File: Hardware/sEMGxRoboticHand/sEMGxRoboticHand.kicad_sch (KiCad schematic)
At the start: 49 parts, among them U1 ADS1298xPAG, U2 ESP32-S3, U3 ADS1298xPAG

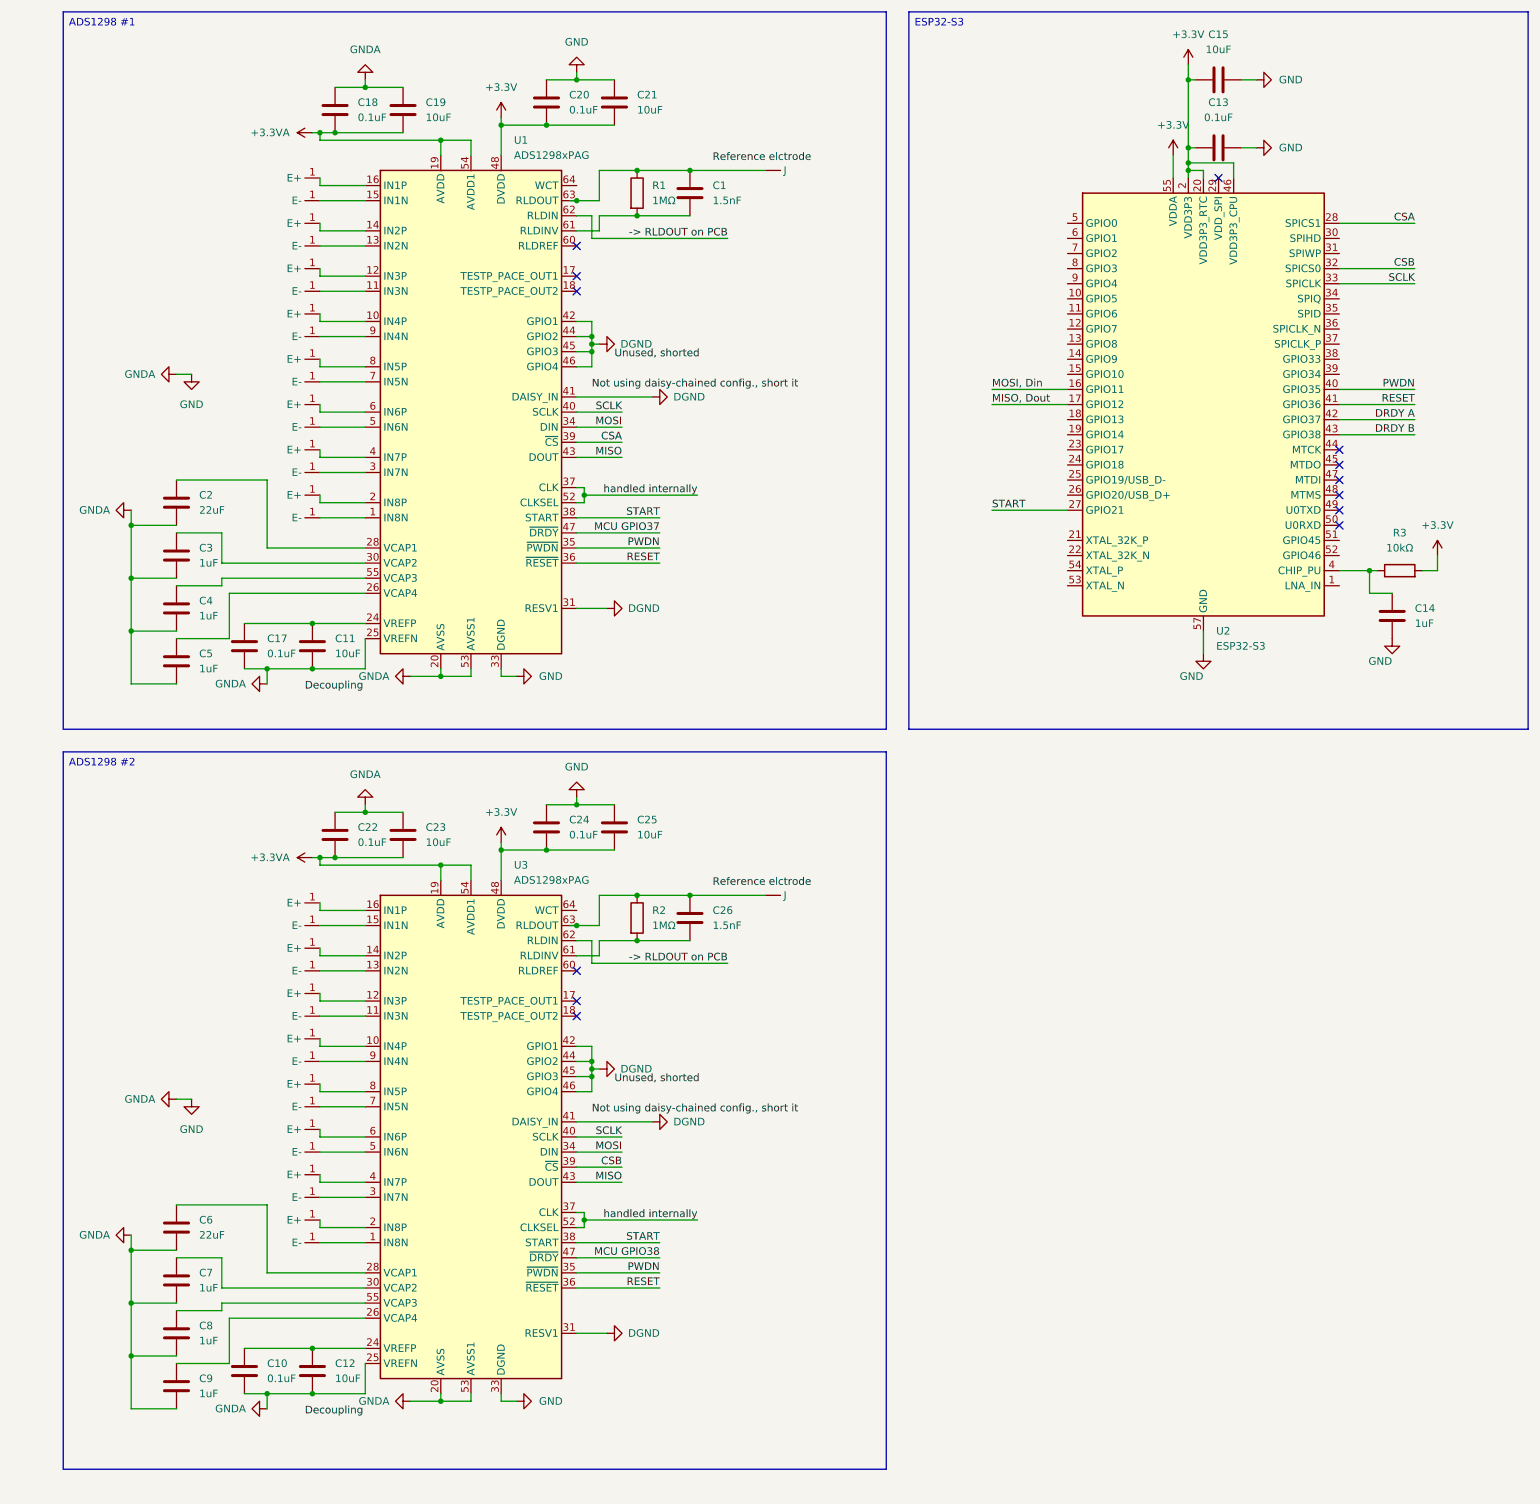
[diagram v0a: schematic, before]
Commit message: [style] Update Design
- Update labelling of "GNDA" to "AGND"
- Update arrow pointing directions of GNDs and Voltage supplies following convention
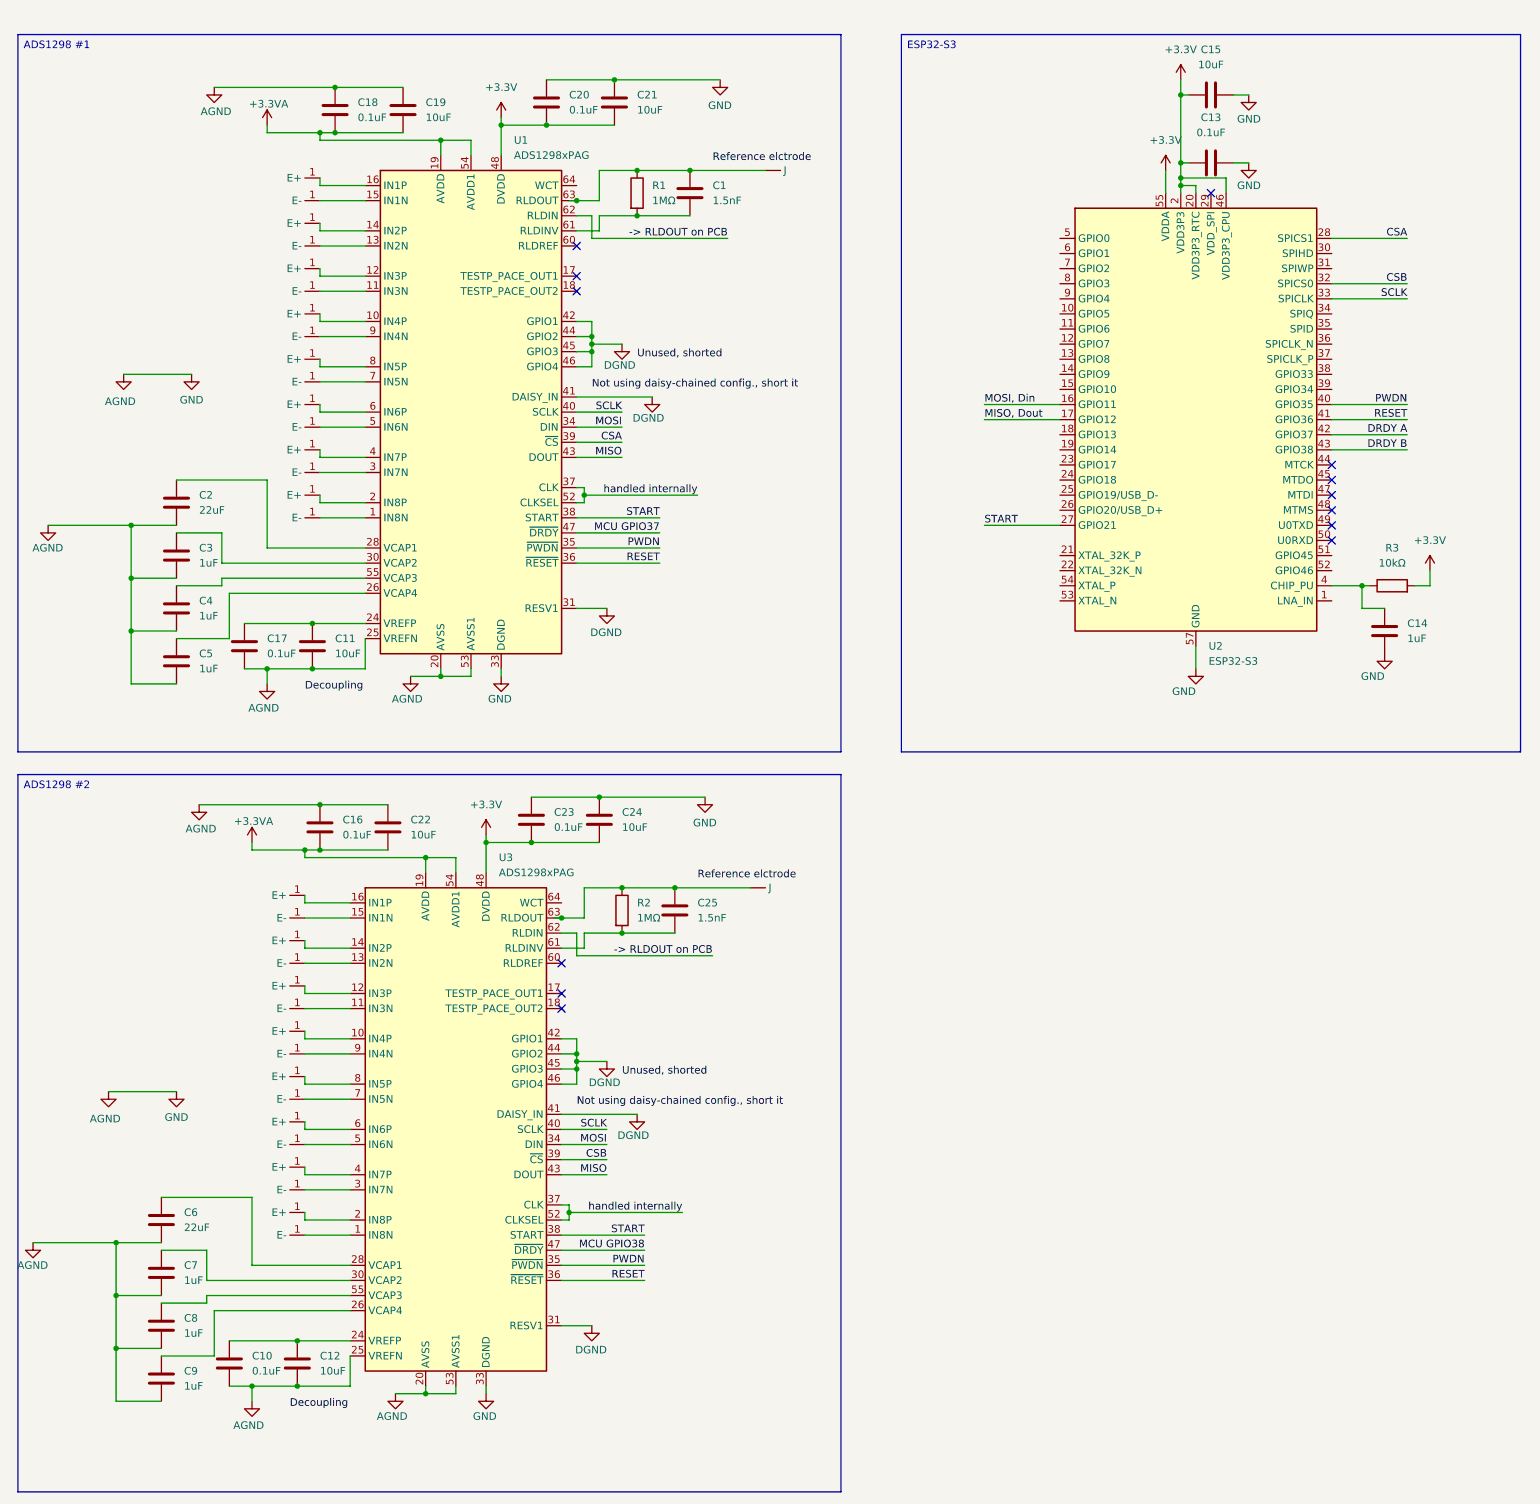
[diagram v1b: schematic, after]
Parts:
- removed C26: 1.5nF, symbol Device:C
- added C16: 0.1uF, symbol Device:C
- C22, C24: value 0.1uF -> 10uF
- C23: value 10uF -> 0.1uF
- C25: value 10uF -> 1.5nF
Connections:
- net +3.3V: now also C23.2; no longer C25.2
- net +3.3VA: now also C16.2; no longer C23.2
- net at R2.1, U3.63 (RLDOUT), U5. (J): now also C25.1
- net at R2.2, U3.61 (RLDINV): now also C25.2
- net GND renamed AGND
- net AGND: now also C16.1; no longer C25.1
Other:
- moved on the sheet: C13, C14, C15, R3, U2

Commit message: [style] Update labels & ports & texts
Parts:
- removed E1: ~, symbol dry_electrode:differential_electrode
- added C26: C, symbol Device:C
- added R4: R, symbol Device:R
- added U6: ESP32-S3-WROOM-1, RF_Module:ESP32-S3-WROOM-1, symbol RF_Module:ESP32-S3-WROOM-1
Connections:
- net MCU GPIO37 is gone; now on net DRDY A: U1.47 (~{DRDY})
- net MCU GPIO38 is gone; now on net DRDY B: U3.47 (~{DRDY})
- net MISO, Dout is gone; now on net MISO: U2.17 (GPIO12)
- net MOSI, Din is gone; now on net MOSI: U2.16 (GPIO11)
- net at U1.15 (IN1N): now also C26.2
- net at U1.16 (IN1P): now also C26.1, R4.2
- net -> RLDOUT on PCB: no longer names the net of U3.62 (RLDIN)
- net -> RLDOUT on PCB: no longer U1.62 (RLDIN)
- net handled internally: no longer names the net of U3.37 (CLK), U3.52 (CLKSEL)
- net handled internally: no longer U1.37 (CLK), U1.52 (CLKSEL)
- new net: U6.1 (GND), U6.40 (GND), U6.41 (GND)
- new net: U1.37 (CLK), U1.52 (CLKSEL)
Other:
- note added: "Not using daisy-chained config., short it"
- note added: "RLDIN -> RLDOUT on PCB"
- note added: "Reference elctrode"
- note added: "Unused, shorted"
- note added: "handled internally"
- moved on the sheet: C1, C11, C13, C14, C15, C17, C18, C19, C2, C20, C21, C3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

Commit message: [style] Replace electrodes to components
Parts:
- removed E2, E3, E4, E5, E6, E7, E8: ~, symbol dry_electrode:differential_electrode
- added C27, C28, C29, C30, C31, C32, C33: C, symbol Device:C
- added E1+, E1-, E2+, E2-, E3+, E3-, E4+, E4-, E5+, E5-, E6+, E6-, E7+, E7-, E8+, E8-: TestPoint, symbol Connector:TestPoint
- added R10, R11, R12, R13, R14, R15, R16, R17, R18, R19, R5, R6, R7, R8, R9: R, symbol Device:R
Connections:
- net at C26.2, U1.15 (IN1N): now also R5.2
- net at C5.1, U1.26 (VCAP4): now also C3.1, U1.30 (VCAP2)
- net at R4.1: now also E1+.1
- net at U1.7 (IN5N): now also C30.2, R13.2
- net at U1.8 (IN5P): now also C30.1, R12.2
- net at U1.10 (IN4P): now also C29.1, R10.2
- net at U1.9 (IN4N): now also C29.2, R11.2
- net at U1.11 (IN3N): now also C28.2, R9.2
- net at U1.12 (IN3P): now also C28.1, R8.2
- net at U1.13 (IN2N): now also C27.2, R7.2
- net at U1.14 (IN2P): now also C27.1, R6.2
- net at U1.1 (IN8N): now also C33.2, R19.2
- net at U1.2 (IN8P): now also C33.1, R18.2
- net at U1.3 (IN7N): now also C32.2, R17.2
- net at U1.4 (IN7P): now also C32.1, R16.2
- net at U1.5 (IN6N): now also C31.2, R15.2
- net at U1.6 (IN6P): now also C31.1, R14.2
- new net: E6-.1, R15.1
- new net: E4-.1, R11.1
- new net: E7+.1, R16.1
- new net: E3+.1, R8.1
- new net: E1-.1, R5.1
- new net: E2+.1, R6.1
- new net: E5+.1, R12.1
- new net: E7-.1, R17.1
- new net: E3-.1, R9.1
- new net: E4+.1, R10.1
- new net: E8-.1, R19.1
- new net: E2-.1, R7.1
- new net: E6+.1, R14.1
- new net: E5-.1, R13.1
- new net: E8+.1, R18.1
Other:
- moved on the sheet: C1, C10, C11, C12, C13, C14, C15, C16, C17, C18, C19, C2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

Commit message: [style] Update on Schematic
Update on 1 ADS1298 only
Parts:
- removed E1+, E1-, E2+, E2-, E3+, E3-, E4+, E4-, E5+, E5-, E6+, E6-, E7+, E7-, E8+, E8-: TestPoint, symbol Connector:TestPoint
- removed U4: ~, symbol ref_electrode:J
- added C34, C35, C36, C37, C38, C39, C40, C41: 620pF, symbol Device:C
- added E1, E2, E3, E4, E5, E6, E7, E8: Electrodes, symbol Connector:Conn_01x02_Pin
- added J1: Reference Electrode, symbol Connector:Conn_01x01_Pin
- C26, C27, C28, C29, C30, C31, C32, C33: value C -> 620pF
- R10, R11, R12, R13, R14, R15, R16, R17, R18, R19, R4, R5, R6, R7, R8, R9: value R -> 2KΩ
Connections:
- net AGND: now also C26.2, C27.2, C28.2, C29.2, C30.2, C31.2, C32.2, C33.2, C34.2, C35.2, C36.2, C37.2, C38.2, C39.2, C40.2, C41.2
- net at R15.1: now also E6.2 (Pin_2)
- net at R15.2, U1.5 (IN6N): now also C32.1; no longer C31.2
- net at R5.2, U1.15 (IN1N): now also C34.1; no longer C26.2
- net at R11.1: now also E4.2 (Pin_2)
- net at R11.2, U1.9 (IN4N): now also C37.1; no longer C29.2
- net at R16.1: now also E7.1 (Pin_1)
- net at R13.2, U1.7 (IN5N): now also C38.1; no longer C30.2
- net at C5.1, U1.26 (VCAP4): no longer C3.1, U1.30 (VCAP2)
- net at R8.1: now also E3.1 (Pin_1)
- net at R4.1: now also E1.1 (Pin_1)
- net at R16.2, U1.4 (IN7P): now also C33.1; no longer C32.1
- net at R17.2, U1.3 (IN7N): now also C39.1; no longer C32.2
- net at R5.1: now also E1.2 (Pin_2)
- net at R6.1: now also E2.1 (Pin_1)
- net at R12.1: now also E5.1 (Pin_1)
- net at R18.2, U1.2 (IN8P): now also C40.1; no longer C33.1
- net at R19.2, U1.1 (IN8N): now also C41.1; no longer C33.2
- net at C1.1, R1.1, U1.63 (RLDOUT): now also J1.1 (Pin_1)
- net at R17.1: now also E7.2 (Pin_2)
- net at R9.1: now also E3.2 (Pin_2)
- net at R10.1: now also E4.1 (Pin_1)
- net at R19.1: now also E8.2 (Pin_2)
- net at R7.1: now also E2.2 (Pin_2)
- net at R14.1: now also E6.1 (Pin_1)
- net at R9.2, U1.11 (IN3N): now also C36.1; no longer C28.2
- net at R13.1: now also E5.2 (Pin_2)
- net at R18.1: now also E8.1 (Pin_1)
- net at R7.2, U1.13 (IN2N): now also C35.1; no longer C27.2
- new net: C3.1, U1.30 (VCAP2)
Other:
- moved on the sheet: C1, C10, C11, C12, C13, C14, C15, C16, C17, C18, C19, C2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

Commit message: Update on circuit schematic
- Added LDOs & Battery
- Changed to daisy-chained configuration
- Updated MCU to ESP32-S3 Wroom
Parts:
- removed C10, C16, C23: 0.1uF, symbol Device:C
- removed C12, C22, C24: 10uF, symbol Device:C
- removed C25: 1.5nF, symbol Device:C
- removed C6: 22uF, symbol Device:C
- removed C7, C8, C9: 1uF, symbol Device:C
- removed E10, E11, E12, E13, E14, E15, E16, E9: ~, symbol dry_electrode:differential_electrode
- removed R2: 1MΩ, symbol Device:R
- removed U2: ESP32-S3, Package_DFN_QFN:QFN-56-1EP_7x7mm_P0.4mm_EP4x4mm, symbol MCU_Espressif:ESP32-S3
- removed U3: ADS1298xPAG, Package_QFP:TQFP-64_10x10mm_P0.5mm, symbol Analog_ADC:ADS1298xPAG
- removed U5: ~, symbol ref_electrode:J
- added BT1: Battery, symbol Device:Battery
- added C42: 10nF, symbol Device:C
- added C43, C45, C49, C64, C65, C66: 1uF, symbol Device:C
- added C44: 2.2uF, symbol Device:C
- added C46: 200uF, symbol Device:C
- added C47, C63: 22uF, symbol Device:C
- added C48, C67, C69, C71: 0.1uF, symbol Device:C
- added C50, C51, C52, C53, C54, C55, C56, C57, C58, C59, C60, C61, C62: 620pF, symbol Device:C
- added C68, C70, C72: 10uF, symbol Device:C
- added C73: 1.5nF, symbol Device:C
- added E17, E18, E19, E20, E21, E22, E23, E24: Electrodes, symbol Connector:Conn_01x02_Pin
- added J2: Reference Electrode, symbol Connector:Conn_01x01_Pin
- added R20: 10kΩ, symbol Device:R
- added R21, R22, R23, R24, R25, R26, R27, R28, R29, R30, R31, R32, R33, R34, R35: 2KΩ, symbol Device:R
- added R36: 1MΩ, symbol Device:R
- added U2: ADS1298xPAG, Package_QFP:TQFP-64_10x10mm_P0.5mm, symbol Analog_ADC:ADS1298xPAG
- added U4: LP2985-3.3, Package_TO_SOT_SMD:SOT-23-5, symbol Regulator_Linear:LP2985-3.3
- added U7: TLV75533PDBV, Package_TO_SOT_SMD:SOT-23-5, symbol Regulator_Linear:TLV75533PDBV
- C13: value 0.1uF -> 620pF
- C14: value 1uF -> 620pF
- C15: value 10uF -> 620pF
- R3: value 10kΩ -> 2KΩ
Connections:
- net CSA is gone; now on net CS: U1.39 (~{CS})
- net +3.3V: now also U6.2 (3V3), C44.1, C46.1, C47.1, C48.1, C71.2, C72.2, R20.2, U2.48 (DVDD), U2.50 (DVDD), U4.5 (VOUT), U7.5 (OUT); no longer C13.1, C15.1, R3.2
- net +3.3VA: now also C69.2, C70.2, U2.19 (AVDD), U2.21 (AVDD), U2.22 (AVDD), U2.54 (AVDD1), U2.56 (AVDD), U2.59 (AVDD)
- net AGND: now also U6.1 (GND), U6.40 (GND), U6.41 (GND), BT1.2 (-), C42.2, C43.2, C44.2, C45.2, C46.2, C47.2, C48.2, C49.2, C50.2, C51.2, C52.2, C53.2, C54.2, C55.2, C56.2, C57.2, C58.2, C59.2, C60.2, C61.2, C62.2, C63.2, C64.2, C65.2, C66.2, C67.2, C68.2, C69.1, C70.1, C71.1, C72.1, U2.20 (AVSS), U2.23 (AVSS), U2.25 (VREFN), U2.32 (AVSS), U2.33 (DGND), U2.49 (DGND), U2.51 (DGND), U2.53 (AVSS1), U2.57 (AVSS), U2.58 (AVSS), U4.2 (GND), U7.2 (GND)
- net DGND: now also U2.31 (RESV1), U2.42 (GPIO1), U2.44 (GPIO2), U2.45 (GPIO3), U2.46 (GPIO4)
- net MISO: now also U6.20 (IO12), U2.43 (DOUT); no longer U1.43 (DOUT)
- net MOSI: now also U6.19 (IO11), U2.34 (DIN)
- net PWDN: now also U6.6 (IO6), U2.35 (~{PWDN})
- net RESET: now also U6.7 (IO7), U2.36 (~{RESET})
- net SCLK: now also U6.21 (IO13), U2.40 (SCLK)
- net START: now also U6.23 (IO21), U2.38 (START)
- net at C14.1: now also R21.2, U2.15 (IN1N); no longer R3.1
- net DRDY: now reaches U6.12 (IO8)
- net DRDY: now also U2.47 (~{DRDY})
- net at U6.3 (EN): now also C49.1, R20.1
- net CS: now reaches U6.5 (IO5)
- net CS: now also U2.39 (~{CS})
- net DRDY A: no longer names the net of U1.47 (~{DRDY})
- new net: C57.1, R30.2, U2.6 (IN6P)
- new net: E20.1 (Pin_1), R26.1
- new net: E20.2 (Pin_2), R27.1
- new net: C42.1, U4.4 (BP)
- new net: C53.1, R26.2, U2.10 (IN4P)
- new net: E21.2 (Pin_2), R29.1
- new net: C56.1, R29.2, U2.7 (IN5N)
- new net: C54.1, R27.2, U2.9 (IN4N)
- new net: C52.1, R25.2, U2.11 (IN3N)
- new net: C61.1, R34.2, U2.2 (IN8P)
- new net: C63.1, U2.28 (VCAP1)
- new net: E24.1 (Pin_1), R34.1
- new net: E24.2 (Pin_2), R35.1
- new net: C73.1, J2.1 (Pin_1), R36.1, U2.63 (RLDOUT)
- new net: E18.1 (Pin_1), R22.1
- new net: E18.2 (Pin_2), R23.1
- new net: C58.1, R31.2, U2.5 (IN6N)
- new net: C59.1, R32.2, U2.4 (IN7P)
- new net: C55.1, R28.2, U2.8 (IN5P)
- new net: E22.1 (Pin_1), R30.1
- new net: E22.2 (Pin_2), R31.1
- new net: E19.2 (Pin_2), R25.1
- new net: E19.1 (Pin_1), R24.1
- new net: C51.1, R24.2, U2.12 (IN3P)
- new net: E21.1 (Pin_1), R28.1
- new net: C73.2, R36.2, U2.61 (RLDINV)
- new net: C66.1, U2.26 (VCAP4)
- new net: C60.1, R33.2, U2.3 (IN7N)
- new net: C15.1, R22.2, U2.14 (IN2P)
- new net: C62.1, R35.2, U2.1 (IN8N)
- new net: C64.1, U2.30 (VCAP2)
- new net: E17.2 (Pin_2), R21.1
- new net: E17.1 (Pin_1), R3.1
- new net: C13.1, R3.2, U2.16 (IN1P)
- new net: E23.2 (Pin_2), R33.1
- new net: E23.1 (Pin_1), R32.1
- new net: C67.1, C68.1, U2.24 (VREFP)
- new net: C50.1, R23.2, U2.13 (IN2N)
- new net: U2.37 (CLK), U2.52 (CLKSEL)
- new net: C65.1, U2.55 (VCAP3)
- new net +3.7V: BT1.1 (+), C43.1, C45.1, U4.1 (VIN), U7.1 (IN)
- new net DAISY_CHAIN_B: U1.43 (DOUT), U2.41 (DAISY_IN)
- new net EN: U4.3 (ON/~{OFF}), U7.3 (EN)
- no-connect marks 13 -> 6
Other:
- note removed: "Not using daisy-chained config., short it"
- note removed: "Reference elctrode"
- moved on the sheet: C1, C11, C17, C18, C19, C2, C20, C21, C26, C27, C28, C29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
